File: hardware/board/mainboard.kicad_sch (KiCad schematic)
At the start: 0 parts

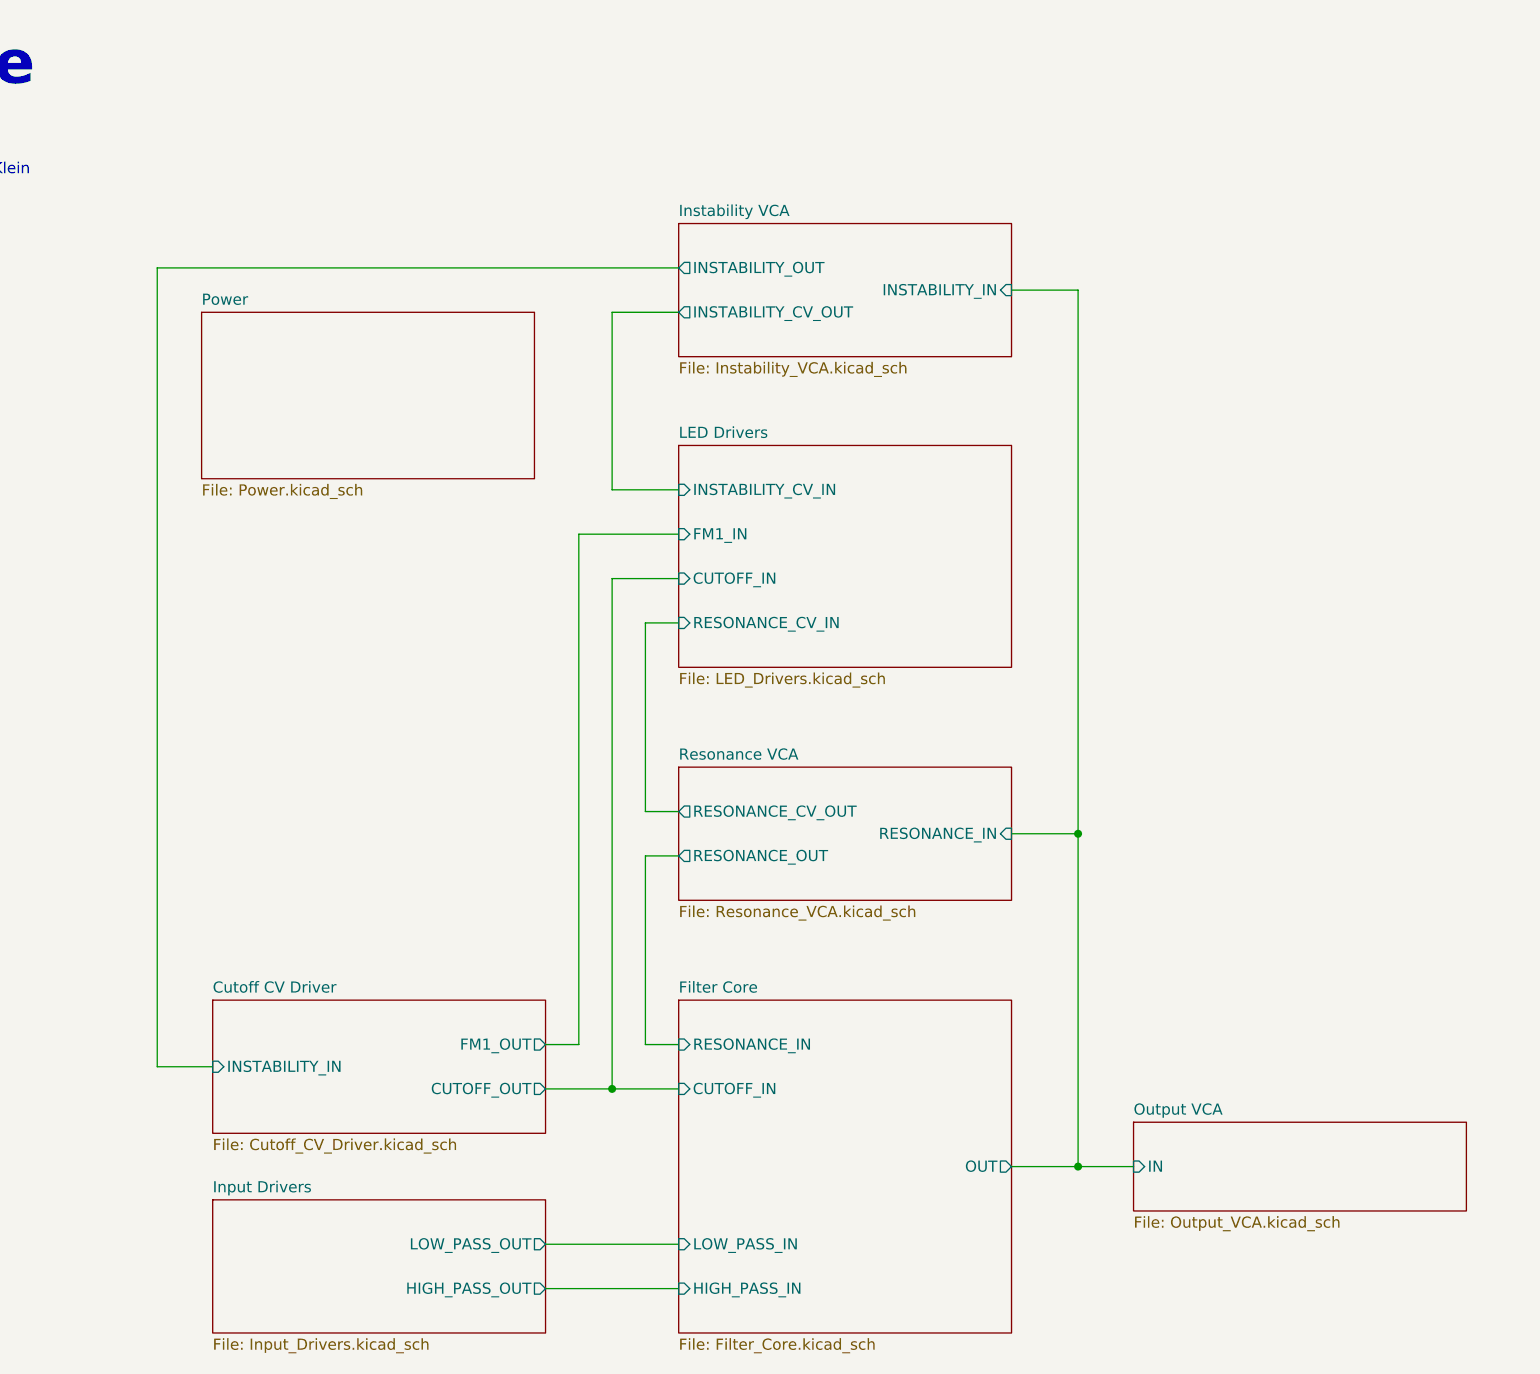
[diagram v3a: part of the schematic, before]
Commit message: Few cleanups for LED drivers
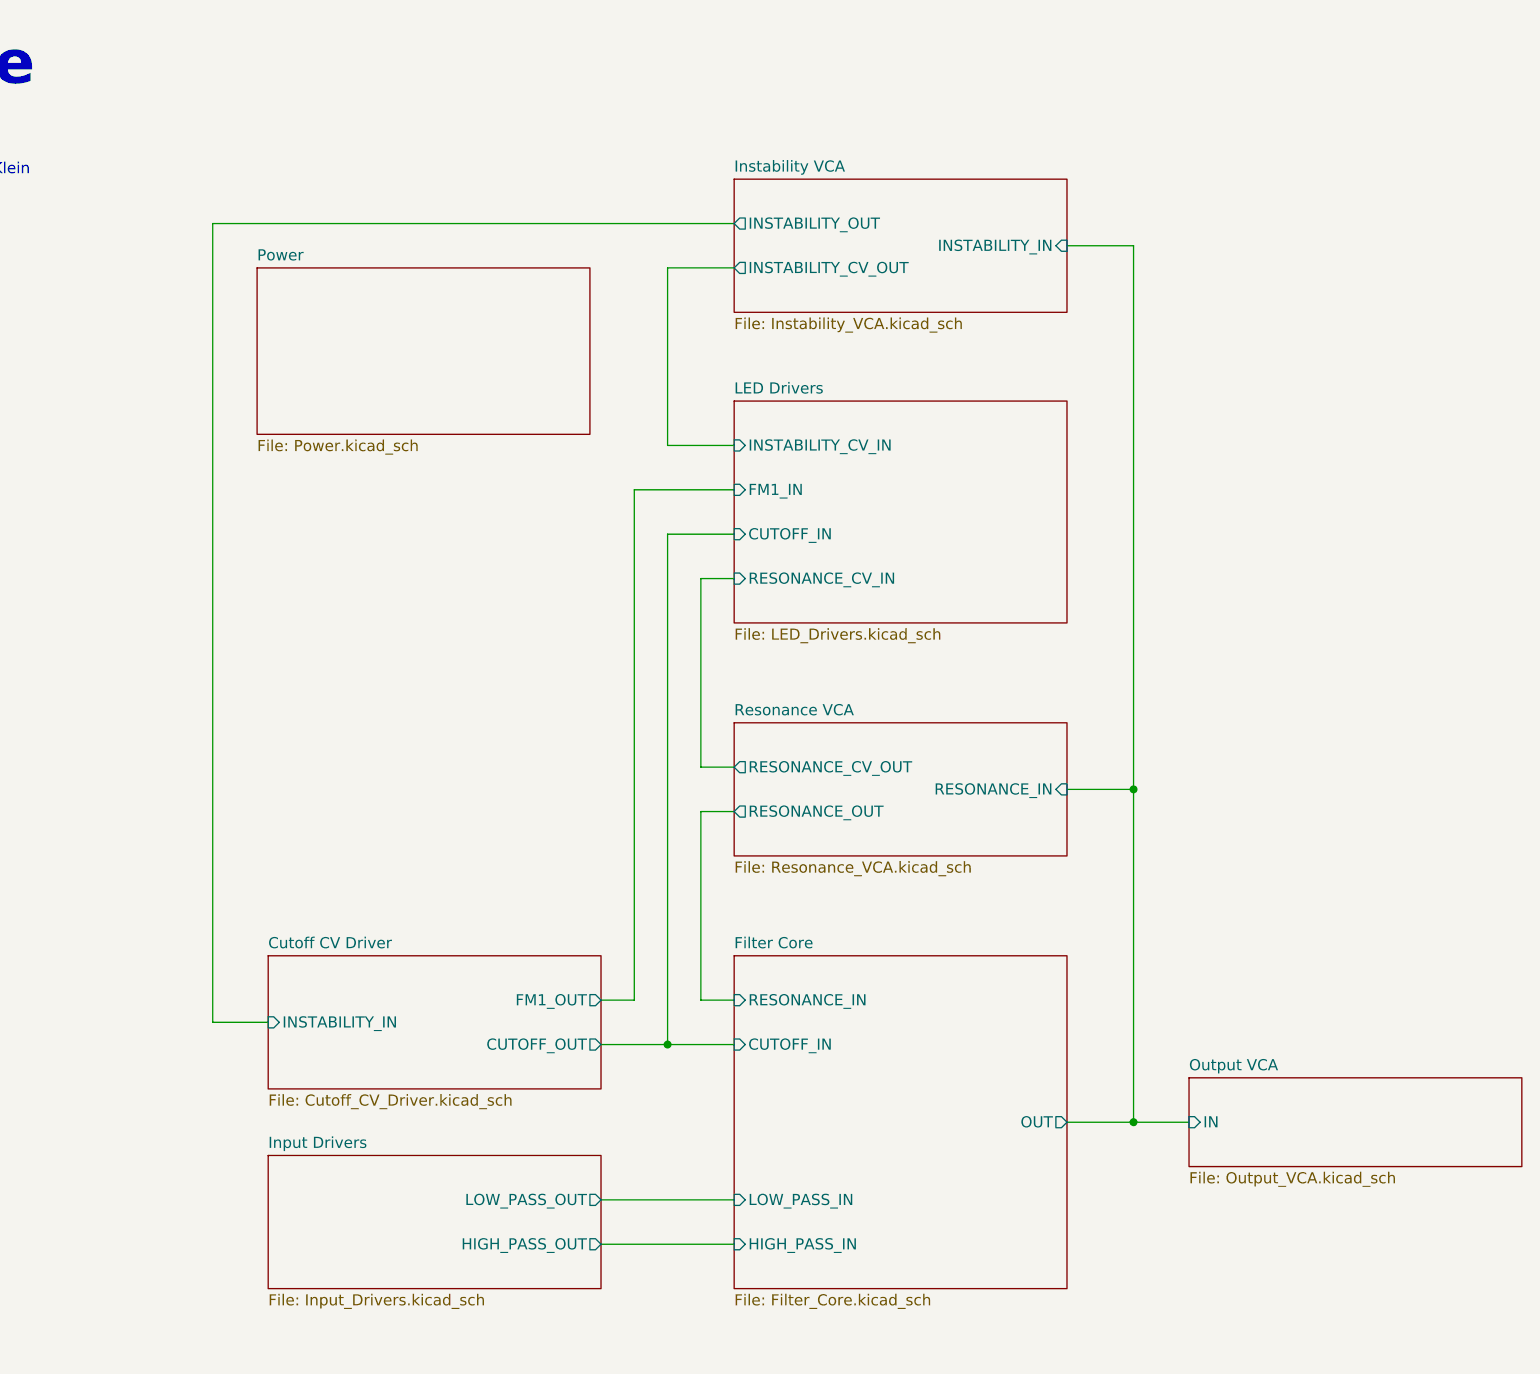
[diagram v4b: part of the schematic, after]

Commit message: hardware: update schematic with footprints and preliminary MPNs
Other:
- title: Diode Ladder Filter -> Neptune
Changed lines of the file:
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@@
   (paper "USLetter")
   (title_block
-    (title "Diode Ladder Filter")
-    (date "2023-06-08")
-    (rev "v0.1")
+    (title "Neptune")
+    (date "2023-07-20")
+    (rev "v0")
     (company "Winterbloom")
     (comment 1 "Carson Walls")
-    (comment 2 "LICENSE TBD")
-    (comment 3 "TBD.wntr.dev")
+    (comment 2 "CERN-OHL-P v2")
+    (comment 3 "neptune.wntr.dev")
   )
   (junction (at 176.53 143.51) (diameter 0) (color 0 0 0 0)
@@
     (instances
       (project "mainboard"
+        (path "/960bd036-bf0c-45ea-9f41-1321756e0e5a" (page "7"))
+      )
+    )
+  )
+  (sheet (at 76.2 45.72) (size 38.1 19.05) (fields_autoplaced)
+    (stroke (width 0.1524) (type solid))
+    (fill (color 0 0 0 0.0000))
+    (property "Sheetname" "Power" (at 76.2 45.0084 0)
+      (effects (font (size 1.27 1.27)) (justify left bottom))
+    )
+    (property "Sheetfile" "Power.kicad_sch" (at 76.2 65.3546 0)
+      (effects (font (size 1.27 1.27)) (justify left top))
+    )
+    (instances
+      (project "mainboard"
+        (path "/960bd036-bf0c-45ea-9f41-1321756e0e5a" (page "2"))
+      )
+    )
+  )
+  (sheet (at 77.47 147.32) (size 38.1 15.24) (fields_autoplaced)
+    (stroke (width 0.1524) (type solid))
+    (fill (color 0 0 0 0.0000))
+    (property "Sheetname" "Input Drivers" (at 77.47 146.6084 0)
+      (effects (font (size 1.27 1.27)) (justify left bottom))
+    )
+    (property "Sheetfile" "Input_Drivers.kicad_sch" (at 77.47 163.1446 0)
+      (effects (font (size 1.27 1.27)) (justify left top))
+    )
+    (pin "HIGH_PASS_OUT" output (at 115.57 157.48 0)
+      (effects (font (size 1.27 1.27)) (justify right))
+    )
+    (pin "LOW_PASS_OUT" output (at 115.57 152.4 0)
+      (effects (font (size 1.27 1.27)) (justify right))
+    )
+    (instances
+      (project "mainboard"
+        (path "/960bd036-bf0c-45ea-9f41-1321756e0e5a" (page "2"))
+      )
+    )
+  )
+  (sheet (at 130.81 124.46) (size 38.1 38.1) (fields_autoplaced)
+    (stroke (width 0.1524) (type solid))
+    (fill (color 0 0 0 0.0000))
+    (property "Sheetname" "Filter Core" (at 130.81 123.7484 0)
+      (effects (font (size 1.27 1.27)) (justify left bottom))
+    )
+    (property "Sheetfile" "Filter_Core.kicad_sch" (at 130.81 163.1446 0)
+      (effects (font (size 1.27 1.27)) (justify left top))
+    )
+    (pin "CUTOFF_IN" input (at 130.81 134.62 180)
+      (effects (font (size 1.27 1.27)) (justify left))
+    )
+    (pin "OUT" output (at 168.91 143.51 0)
+      (effects (font (size 1.27 1.27)) (justify right))
+    )
+    (pin "HIGH_PASS_IN" input (at 130.81 157.48 180)
+      (effects (font (size 1.27 1.27)) (justify left))
+    )
+    (pin "RESONANCE_IN" input (at 130.81 129.54 180)
+      (effects (font (size 1.27 1.27)) (justify left))
+    )
+    (pin "LOW_PASS_IN" input (at 130.81 152.4 180)
+      (effects (font (size 1.27 1.27)) (justify left))
+    )
+    (instances
+      (project "mainboard"
         (path "/960bd036-bf0c-45ea-9f41-1321756e0e5a" (page "4"))
       )
     )
-  )
-  (sheet (at 76.2 45.72) (size 38.1 19.05) (fields_autoplaced)
-    (stroke (width 0.1524) (type solid))
-    (fill (color 0 0 0 0.0000))
-    (property "Sheetname" "Power" (at 76.2 45.0084 0)
-      (effects (font (size 1.27 1.27)) (justify left bottom))
-    )
-    (property "Sheetfile" "Power.kicad_sch" (at 76.2 65.3546 0)
-      (effects (font (size 1.27 1.27)) (justify left top))
-    )
-    (instances
-      (project "mainboard"
-        (path "/960bd036-bf0c-45ea-9f41-1321756e0e5a" (page "7"))
-      )
-    )
-  )
-  (sheet (at 77.47 147.32) (size 38.1 15.24) (fields_autoplaced)
-    (stroke (width 0.1524) (type solid))
-    (fill (color 0 0 0 0.0000))
-    (property "Sheetname" "Input Drivers" (at 77.47 146.6084 0)
-      (effects (font (size 1.27 1.27)) (justify left bottom))
-    )
-    (property "Sheetfile" "Input_Drivers.kicad_sch" (at 77.47 163.1446 0)
-      (effects (font (size 1.27 1.27)) (justify left top))
-    )
-    (pin "HIGH_PASS_OUT" output (at 115.57 157.48 0)
-      (effects (font (size 1.27 1.27)) (justify right))
-    )
-    (pin "LOW_PASS_OUT" output (at 115.57 152.4 0)
-      (effects (font (size 1.27 1.27)) (justify right))
-    )
-    (instances
-      (project "mainboard"
-        (path "/960bd036-bf0c-45ea-9f41-1321756e0e5a" (page "9"))
-      )
-    )
-  )
-  (sheet (at 130.81 124.46) (size 38.1 38.1) (fields_autoplaced)
-    (stroke (width 0.1524) (type solid))
-    (fill (color 0 0 0 0.0000))
-    (property "Sheetname" "Filter Core" (at 130.81 123.7484 0)
-      (effects (font (size 1.27 1.27)) (justify left bottom))
-    )
-    (property "Sheetfile" "Filter_Core.kicad_sch" (at 130.81 163.1446 0)
-      (effects (font (size 1.27 1.27)) (justify left top))
-    )
-    (pin "CUTOFF_IN" input (at 130.81 134.62 180)
-      (effects (font (size 1.27 1.27)) (justify left))
-    )
-    (pin "OUT" output (at 168.91 143.51 0)
-      (effects (font (size 1.27 1.27)) (justify right))
-    )
-    (pin "HIGH_PASS_IN" input (at 130.81 157.48 180)
-      (effects (font (size 1.27 1.27)) (justify left))
-    )
-    (pin "RESONANCE_IN" input (at 130.81 129.54 180)
-      (effects (font (size 1.27 1.27)) (justify left))
-    )
-    (pin "LOW_PASS_IN" input (at 130.81 152.4 180)
-      (effects (font (size 1.27 1.27)) (justify left))
-    )
-    (instances
-      (project "mainboard"
-        (path "/960bd036-bf0c-45ea-9f41-1321756e0e5a" (page "2"))
-      )
-    )

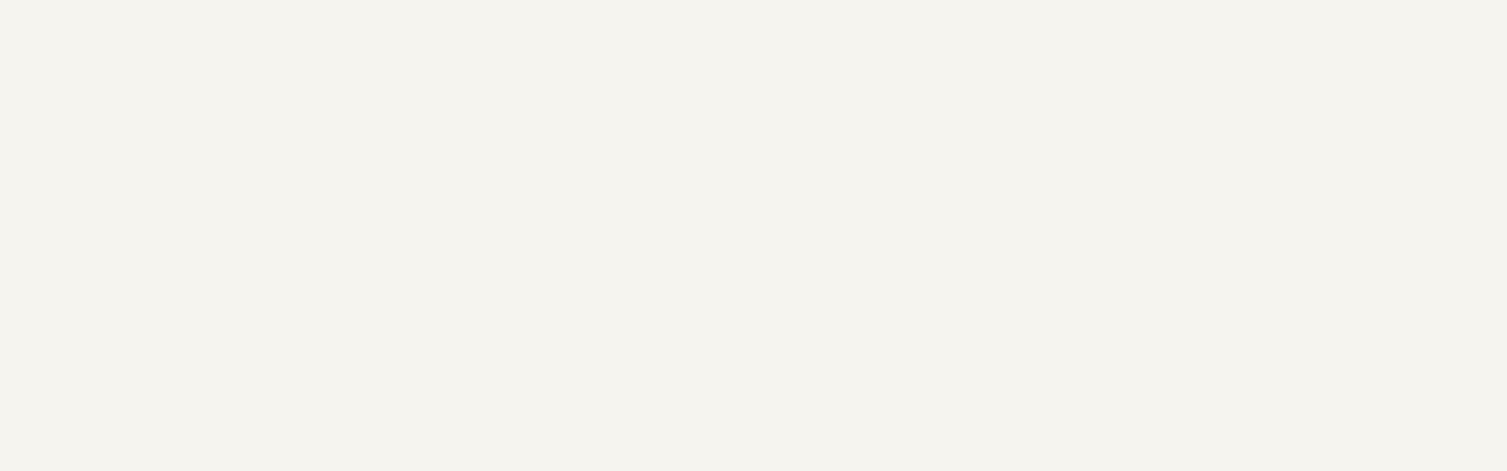
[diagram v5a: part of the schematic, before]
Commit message: Updated Schematic
-Added R935, R936, and Q901 to make resonance self oscillation LED turn on sharply

-Moved D929, D930, and added R933, R934 to make FM1 LED more sensitive

-Changed FM1 Attenuverter and added R410 and R411 to make FM1 Knob have some curve/deadzone

-Changed Resonance VCA output and added R623 and R624 to make resonance VCA output higher voltage to avoid opamp offset being significant .

-Added testing documents
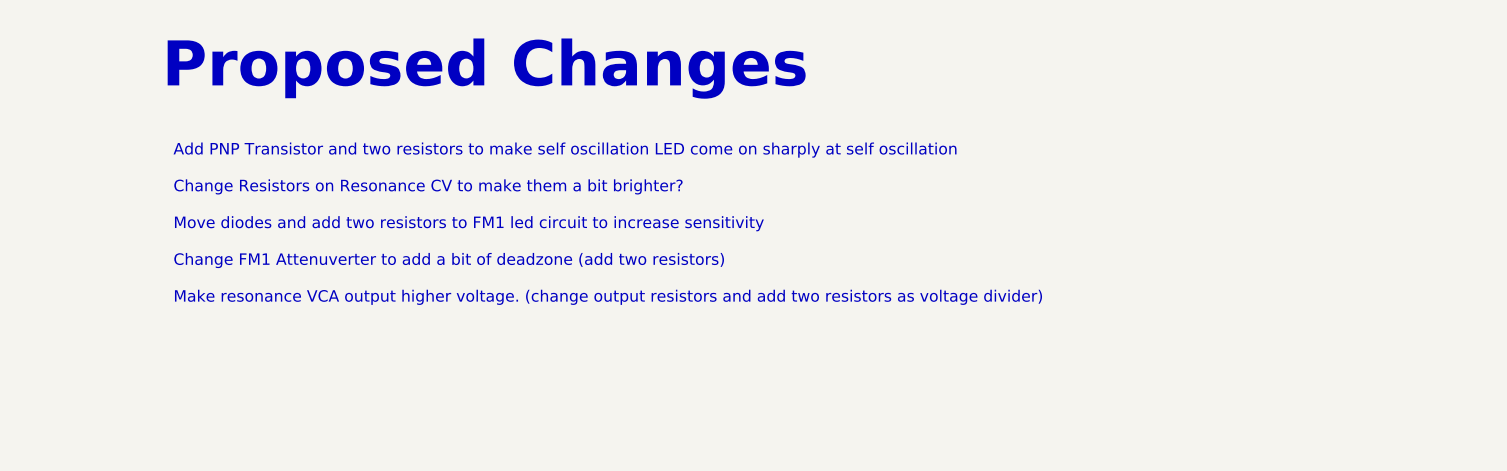
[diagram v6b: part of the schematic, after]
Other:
- note added: "Add PNP Transistor and two resistors to make self oscillation LED come on sharply at self oscillation Change Resistors on Resonance CV to make them a bit brighter? Move diodes and add two resistors to FM1 led circuit to increase sensitivity Change FM1 Attenuverter to add a bit of deadzone (add two resistors) Make resonance VCA output higher voltage. (change output resistors and add two resistors 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"
- note added: "Proposed Changes"
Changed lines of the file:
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@@
     (stroke (width 0) (type default))
+  )
+  (text "Proposed Changes" (at 71.12 -25.4 0)
+    (effects (font (size 5 5) (thickness 0.508) bold) (justify left bottom))
   )
   (text "Neptune" (at 17.78 25.4 0)
     (effects (font (size 5 5) (thickness 0.508) bold) (justify left bottom))
   )
+  (text "Add PNP Transistor and two resistors to make self oscillation LED come on sharply at self oscillation\n\nChange Resistors on Resonance CV to make them a bit brighter?\n\nMove diodes and add two resistors to FM1 led circuit to increase sensitivity\n\nChange FM1 Attenuverter to add a bit of deadzone (add two resistors)\n\nMake resonance VCA output higher voltage. (change output resistors and add two resistors as voltage divider)\n\n\n\n\n"
+    (at 72.39 6.35 0)
+    (effects (font (size 1.27 1.27)) (justify left bottom))
+  )
   (text "4 Pole Diode Ladder Filter\n\nInspired by the filter by Moritz Klein\n\n\n"

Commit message: Slight tweaks
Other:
- note removed: "Add PNP Transistor and two resistors to make self oscillation LED come on sharply at self oscillation Change Resistors on Resonance CV to make them a bit brighter? Move diodes and add two resistors to FM1 led circuit to increase sensitivity Change FM1 Attenuverter to add a bit of deadzone (add two resistors) Make resonance VCA output higher voltage. (change output resistors and add two resistors 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"
- note removed: "Proposed Changes"
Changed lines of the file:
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@@
     (stroke (width 0) (type default))
-  )
-  (text "Proposed Changes" (at 71.12 -25.4 0)
-    (effects (font (size 5 5) (thickness 0.508) bold) (justify left bottom))
   )
   (text "Neptune" (at 17.78 25.4 0)
     (effects (font (size 5 5) (thickness 0.508) bold) (justify left bottom))
   )
-  (text "Add PNP Transistor and two resistors to make self oscillation LED come on sharply at self oscillation\n\nChange Resistors on Resonance CV to make them a bit brighter?\n\nMove diodes and add two resistors to FM1 led circuit to increase sensitivity\n\nChange FM1 Attenuverter to add a bit of deadzone (add two resistors)\n\nMake resonance VCA output higher voltage. (change output resistors and add two resistors as voltage divider)\n\n\n\n\n"
-    (at 72.39 6.35 0)
-    (effects (font (size 1.27 1.27)) (justify left bottom))
-  )
   (text "4 Pole Diode Ladder Filter\n\nInspired by the filter by Moritz Klein\n\n\n"
